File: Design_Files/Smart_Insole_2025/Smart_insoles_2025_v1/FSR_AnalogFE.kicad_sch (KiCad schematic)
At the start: 27 parts, among them U3 MCP6004, U5 MCP6004

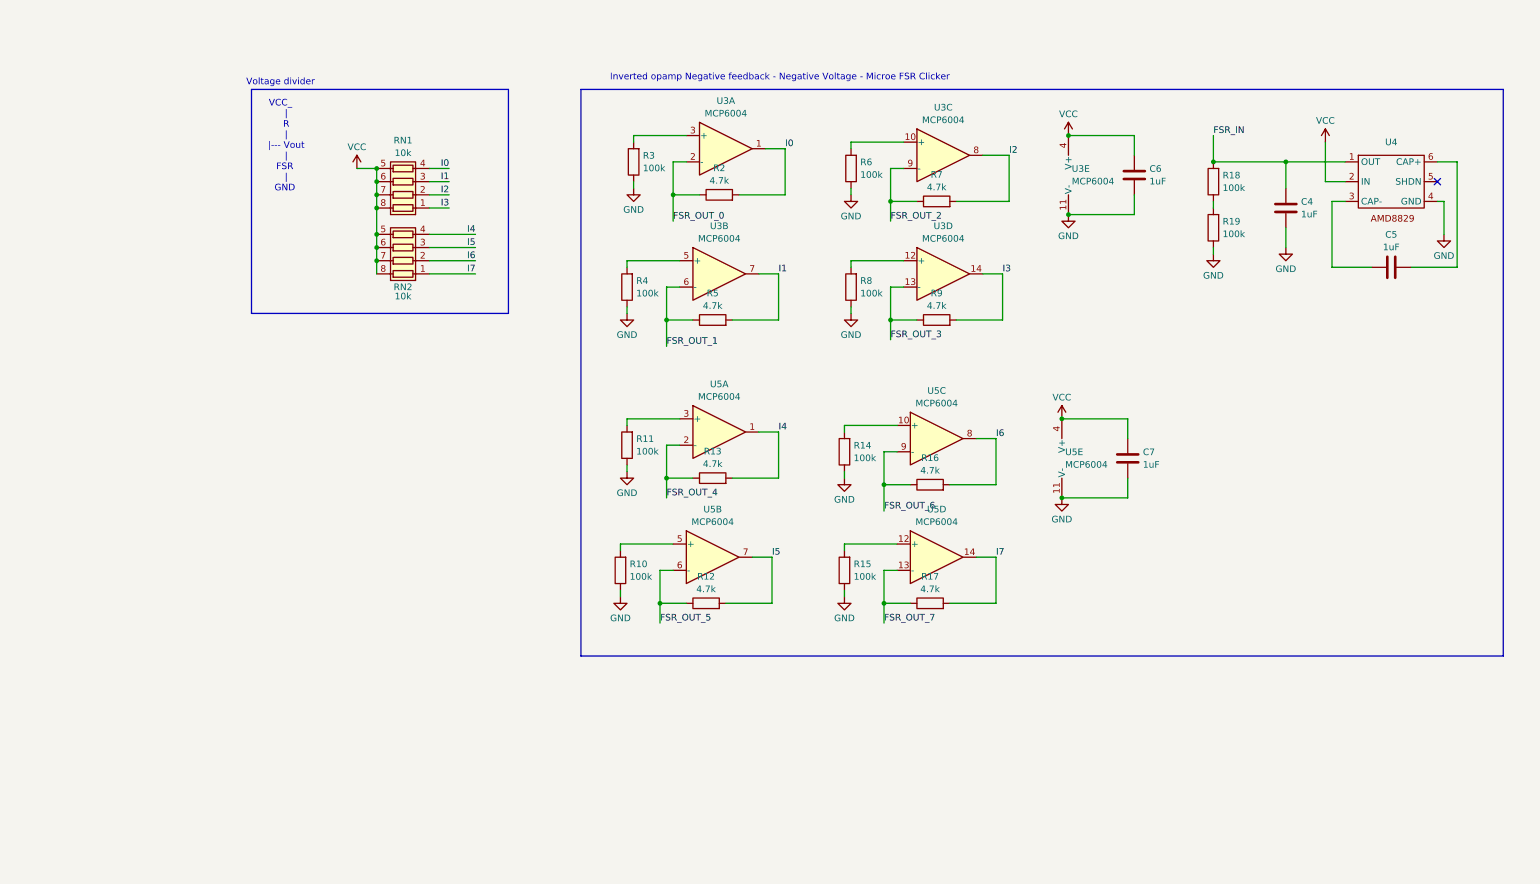
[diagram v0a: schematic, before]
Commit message: Added different AFE circuits to the schematic. Needs verification
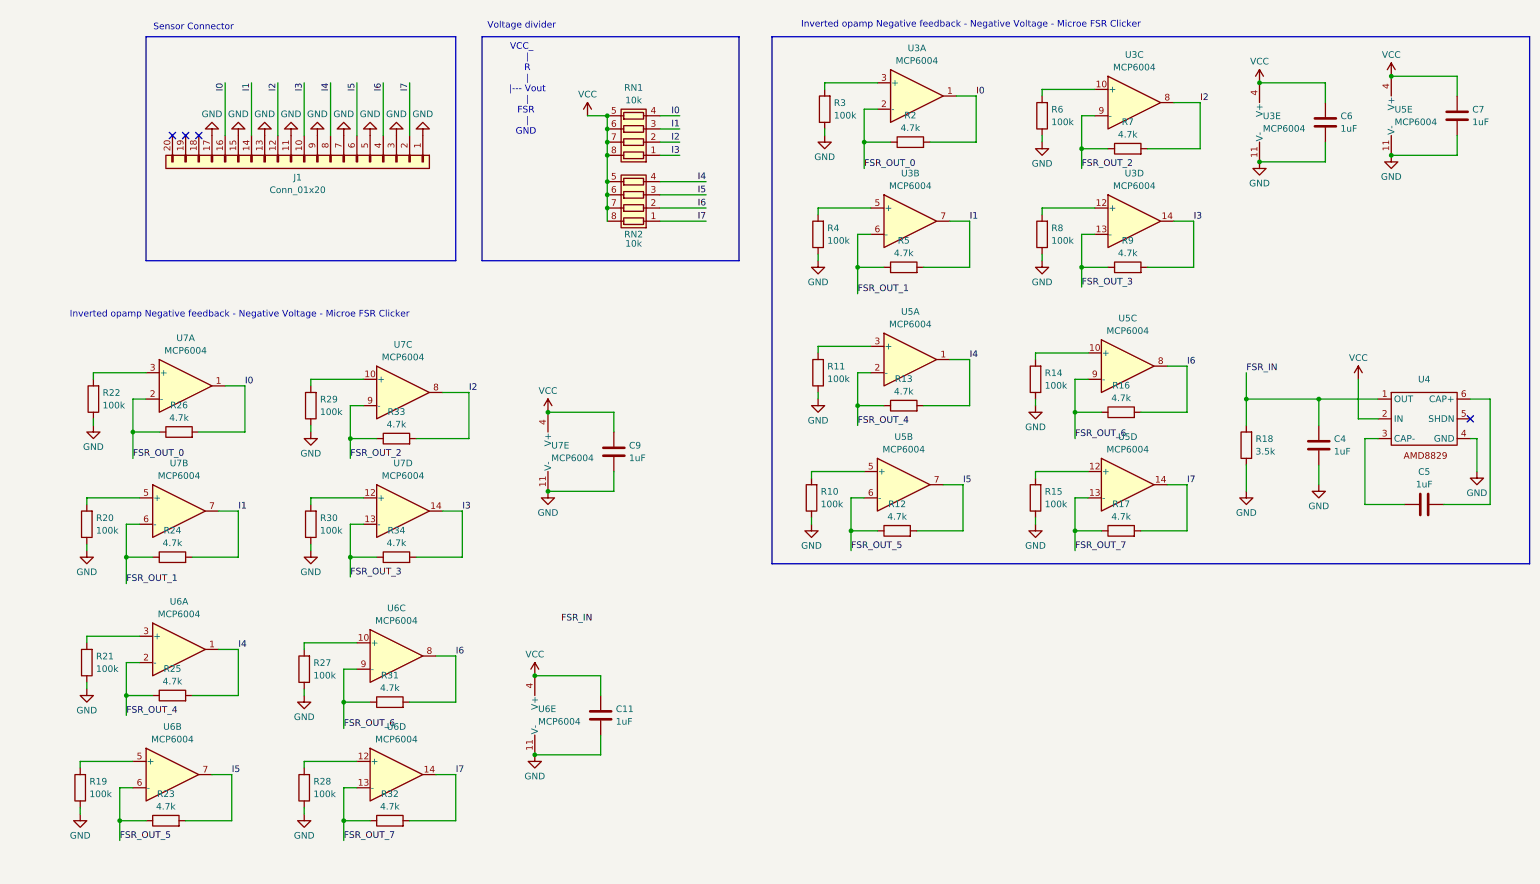
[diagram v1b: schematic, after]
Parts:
- added C11, C9: 1uF, Capacitor_SMD:C_0603_1608Metric_Pad1.08x0.95mm_HandSolder, symbol Device:C
- added J1: Conn_01x20, Connector_Samtec_MicroMate:Samtec_T1M-20-X-S-RA_1x20-1MP_P1.0mm_Terminal_Horizontal, symbol Connector_Generic:Conn_01x20
- added R20, R21, R22, R27, R28, R29, R30: 100k, Resistor_SMD:R_0603_1608Metric_Pad0.98x0.95mm_HandSolder, symbol Device:R
- added R23, R24, R25, R26, R31, R32, R33, R34: 4.7k, Resistor_SMD:R_0603_1608Metric_Pad0.98x0.95mm_HandSolder, symbol Device:R
- added U6, U7: MCP6004, symbol Amplifier_Operational:MCP6004
- R18: value 100k -> 3.5k
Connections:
- net FSR_OUT_0: now also R26.1, U7.2 (-)
- net FSR_OUT_1: now also R24.1, U7.6 (-)
- net FSR_OUT_2: now also R33.1, U7.9 (-)
- net FSR_OUT_3: now also R34.1, U7.13 (-)
- net FSR_OUT_4: now also R25.1, U6.2 (-)
- net FSR_OUT_5: now also R23.1, U6.6 (-)
- net FSR_OUT_6: now also R31.1, U6.9 (-)
- net FSR_OUT_7: now also R32.1, U6.13 (-)
- net GND: now also R18.1, C11.2, C9.2, J1.1 (Pin_1), J1.11 (Pin_11), J1.13 (Pin_13), J1.15 (Pin_15), J1.17 (Pin_17), J1.3 (Pin_3), J1.5 (Pin_5), J1.7 (Pin_7), J1.9 (Pin_9), R20.1, R21.1, R22.1, R27.1, R28.1, R29.1, R30.1, U6.11 (V-), U7.11 (V-)
- net I0: now also J1.16 (Pin_16), R26.2, U7.1
- net I1: now also J1.14 (Pin_14), R24.2, U7.7
- net I2: now also J1.12 (Pin_12), R33.2, U7.8
- net I3: now also J1.10 (Pin_10), R34.2, U7.14
- net I4: now also J1.8 (Pin_8), R25.2, U6.1
- net I5: now also J1.6 (Pin_6), R23.2, U6.7
- net I6: now also J1.4 (Pin_4), R31.2, U6.8
- net I7: now also J1.2 (Pin_2), R32.2, U6.14
- net VCC: now also C11.1, C9.1, U6.4 (V+), U7.4 (V+)
- net at R19.2: now also U6.5 (+); no longer R18.1
- new net: R21.2, U6.3 (+)
- new net: R27.2, U6.10 (+)
- new net: R29.2, U7.10 (+)
- new net: R30.2, U7.12 (+)
- new net: R20.2, U7.5 (+)
- new net: R28.2, U6.12 (+)
- new net: R22.2, U7.3 (+)
- no-connect marks 1 -> 4
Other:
- note added: "Sensor Connector"
- moved on the sheet: C4, C5, C6, C7, R10, R11, R12, R13, R14, R15, R16, R17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

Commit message: Added capacitor to negative feedback fsr circuit
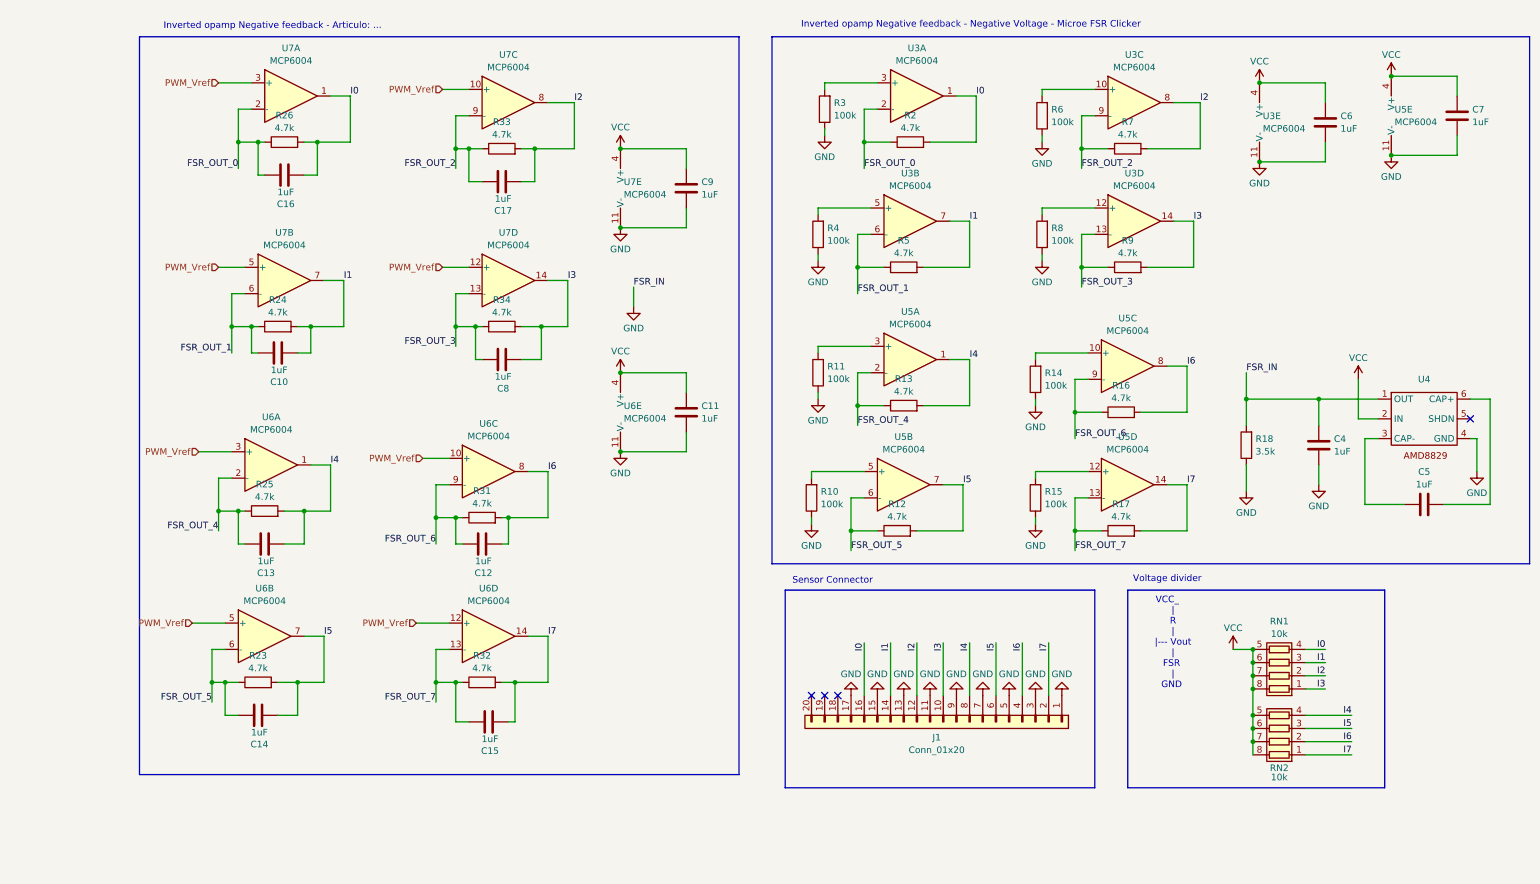
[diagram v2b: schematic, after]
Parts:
- removed R19, R20, R21, R22, R27, R28, R29, R30: 100k, Resistor_SMD:R_0603_1608Metric_Pad0.98x0.95mm_HandSolder, symbol Device:R
- added C10, C12, C13, C14, C15, C16, C17, C8: 1uF, Capacitor_SMD:C_0603_1608Metric_Pad1.08x0.95mm_HandSolder, symbol Device:C
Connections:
- net FSR_IN is gone; now on net GND: C4.1, R18.2, U4.1 (OUT)
- net FSR_OUT_0: now also C16.1
- net FSR_OUT_1: now also C10.1
- net FSR_OUT_2: now also C17.1
- net FSR_OUT_3: now also C8.1
- net FSR_OUT_4: now also C13.1
- net FSR_OUT_5: now also C14.1
- net FSR_OUT_6: now also C12.1
- net FSR_OUT_7: now also C15.1
- net I0: now also C16.2
- net I1: now also C10.2
- net I2: now also C17.2
- net I3: now also C8.2
- net I4: now also C13.2
- net I5: now also C14.2
- net I6: now also C12.2
- net I7: now also C15.2
- net PWM_Vref: now reaches U6.3 (+)
- net PWM_Vref: now also U6.10 (+), U6.12 (+), U6.5 (+), U7.10 (+), U7.12 (+), U7.3 (+), U7.5 (+)
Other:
- note added: "Inverted opamp Negative feedback - Articulo: ..."
- moved on the sheet: C11, C9, J1, R23, R24, R25, R26, R31, R32, R33, R34, RN1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

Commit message: Project division to account for multiple AFE conditioning circuit
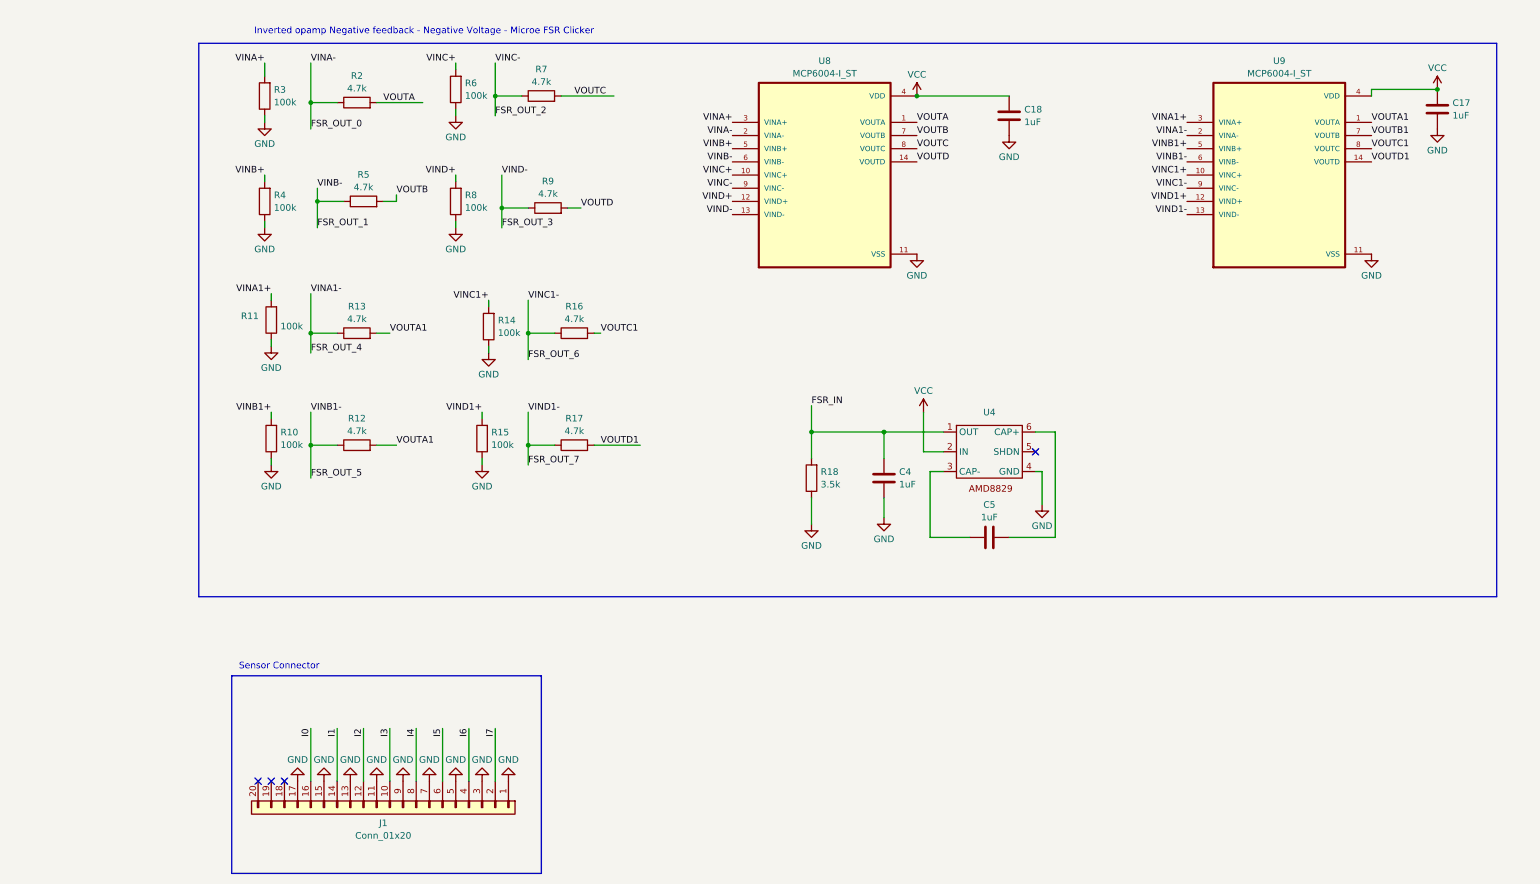
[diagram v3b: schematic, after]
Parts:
- removed C10, C11, C12, C13, C14, C15, C16, C6, C7, C8, C9: 1uF, Capacitor_SMD:C_0603_1608Metric_Pad1.08x0.95mm_HandSolder, symbol Device:C
- removed R23, R24, R25, R26, R31, R32, R33, R34: 4.7k, Resistor_SMD:R_0603_1608Metric_Pad0.98x0.95mm_HandSolder, symbol Device:R
- removed RN1, RN2: 10k, Resistor_SMD:R_Array_Concave_4x0603, symbol Device:R_Pack04
- removed U3, U5, U6, U7: MCP6004, symbol Amplifier_Operational:MCP6004
- added C18: 1uF, Capacitor_SMD:C_0603_1608Metric_Pad1.08x0.95mm_HandSolder, symbol Device:C
- added U8: MCP6004-I_ST, MCP6004_I_ST:SOP65P640X120-14N, symbol MCP6004-I_ST:MCP6004-I_ST
- added U9: MCP6004-I_ST, MCP6004-I_ST:SOP65P640X120-14N, symbol MCP6004-I_ST:MCP6004-I_ST
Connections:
- net FSR_OUT_0: now also U8.2 (VINA-)
- net FSR_OUT_1: now also U8.6 (VINB-)
- net FSR_OUT_2: now also U8.9 (VINC-); no longer C17.1
- net FSR_OUT_3: now also U8.13 (VIND-)
- net FSR_OUT_4: now also U9.2 (VINA-)
- net FSR_OUT_5: now also U9.6 (VINB-)
- net FSR_OUT_6: now also U9.9 (VINC-)
- net FSR_OUT_7: now also U9.13 (VIND-)
- net GND: now also C17.2, C18.2, U8.11 (VSS), U9.11 (VSS); no longer C4.1, R18.2, U4.1 (OUT)
- net I0: no longer R2.2
- net I1: no longer R5.2
- net I2: no longer C17.2, R7.2
- net I3: no longer R9.2
- net I4: no longer R13.2
- net I5: no longer R12.2
- net I6: no longer R16.2
- net I7: no longer R17.2
- net VCC: now also C17.1, C18.1, U8.4 (VDD), U9.4 (VDD)
- net VINB1+: now reaches R10.2
- net VINB1+: now also U9.5 (VINB+)
- net VINC+: now reaches R6.2
- net VINC+: now also U8.10 (VINC+)
- net VINA+: now reaches R3.2
- net VINA+: now also U8.3 (VINA+)
- net VINC1+: now reaches R14.2
- net VINC1+: now also U9.10 (VINC+)
- net VIND1+: now reaches R15.2
- net VIND1+: now also U9.12 (VIND+)
- net VINB+: now reaches R4.2
- net VINB+: now also U8.5 (VINB+)
- net VIND+: now reaches R8.2
- net VIND+: now also U8.12 (VIND+)
- net VINA1+: now reaches R11.2
- net VINA1+: now also U9.3 (VINA+)
- new net FSR_IN: C4.1, R18.2, U4.1 (OUT)
- new net VOUTA: R2.2, U8.1 (VOUTA)
- new net VOUTA1: R12.2, R13.2, U9.1 (VOUTA)
- new net VOUTB: R5.2, U8.7 (VOUTB)
- new net VOUTB1: U9.7 (VOUTB)
- new net VOUTC: R7.2, U8.8 (VOUTC)
- new net VOUTC1: R16.2, U9.8 (VOUTC)
- new net VOUTD: R9.2, U8.14 (VOUTD)
- new net VOUTD1: R17.2, U9.14 (VOUTD)
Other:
- note removed: "Inverted opamp Negative feedback - Articulo: ..."
- note removed: "Voltage divider VCC_ | R | |--- Vout | FSR | GND"
- moved on the sheet: C4, C5, J1, R10, R11, R12, R13, R14, R15, R16, R17, R18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

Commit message: added 3x3 trimpot symbol/footprint. Also Modify schematic to add 3x3trimpots
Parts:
- removed R12, R13, R16, R17, R2, R5, R7, R9: 4.7k, Resistor_SMD:R_0603_1608Metric_Pad0.98x0.95mm_HandSolder, symbol Device:R
- added C10, C11, C12, C13, C6, C7, C8, C9: 10nF, Capacitor_SMD:C_0603_1608Metric_Pad1.08x0.95mm_HandSolder, symbol Device:C
- added R12, R16, R17, R19, R2, R5, R7, R9: TC33X-2-302E, TC33X-2-302E:TRIM_TC33X-2-302E, symbol 3x3TrimPot:TC33X-2-302E
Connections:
- net FSR_OUT_0: now also R2.1
- net FSR_OUT_1: now also C8.1, R5.1
- net FSR_OUT_2: now also C6.1, R7.1
- net FSR_OUT_3: now also C9.1, R9.1
- net FSR_OUT_4: now also C13.1, R12.1
- net FSR_OUT_5: now also C12.1, R17.1
- net FSR_OUT_6: now also C10.1, R19.1
- net FSR_OUT_7: now also C11.1, R16.1
- net VOUTA: now also R2.2, R2.3
- net VOUTA1: now also C12.2, C13.2, R12.2, R12.3, R17.2, R17.3
- net VOUTB: now also C8.2, R5.2, R5.3
- net VOUTC: now also C6.2, R7.2, R7.3
- net VOUTC1: now also C10.2, R19.2, R19.3
- net VOUTD: now also C9.2, R9.2, R9.3
- net VOUTD1: now also C11.2, R16.2, R16.3
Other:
- moved on the sheet: C4, C5, R18, U4
